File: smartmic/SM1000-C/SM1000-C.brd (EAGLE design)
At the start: 65 x 100 mm, 200 parts, among them CN1 HDR100-3, CN10 ST-3509, CN11 HDR100-3, CN12 DF11-16DS, CN2 MOLEX-MINI-B-SMT, CN3 RASM722PX, CN4 RJ-45, CN5 ST-3509, CN6 ST-3509, CN7 ST-3509, CN8 ST-3509, CN9 ST-3509, J1 JMP-2PIN, J3 JMP-2PIN, J4 JMP-2PIN, P1 TPAD50, P10 TPAD50, P11 TPAD50, P12 TPAD50, P13 TPAD50, P14 TPAD50, P15 TPAD50, P16 TPAD50, P17 TPAD50, P18 TPAD50, P19 TPAD50, P2 TPAD50, P20 TPAD50, P3 TPAD50, P4 TPAD50, P5 TPAD50, P6 TPAD50, P7 TPAD50, P8 TPAD50, P9 TPAD50, SW1 SW-BOURNS-7914S, SW2 SW-BOURNS-7914S, SW3 DPDT, SW4 SW-BOURNS-7914S, SW5 SW-BOURNS-7914J, T1 SM-LP-5001, T2 SM-LP-5001, U1 STM32F405, U2 LD3985M33R, U3 STMPS2141, U4 EMIF02-USB03F2, U5 TPS54329E, U6 LMV341, U7 LMV341, U8 LM386M-1, U9 LMV341

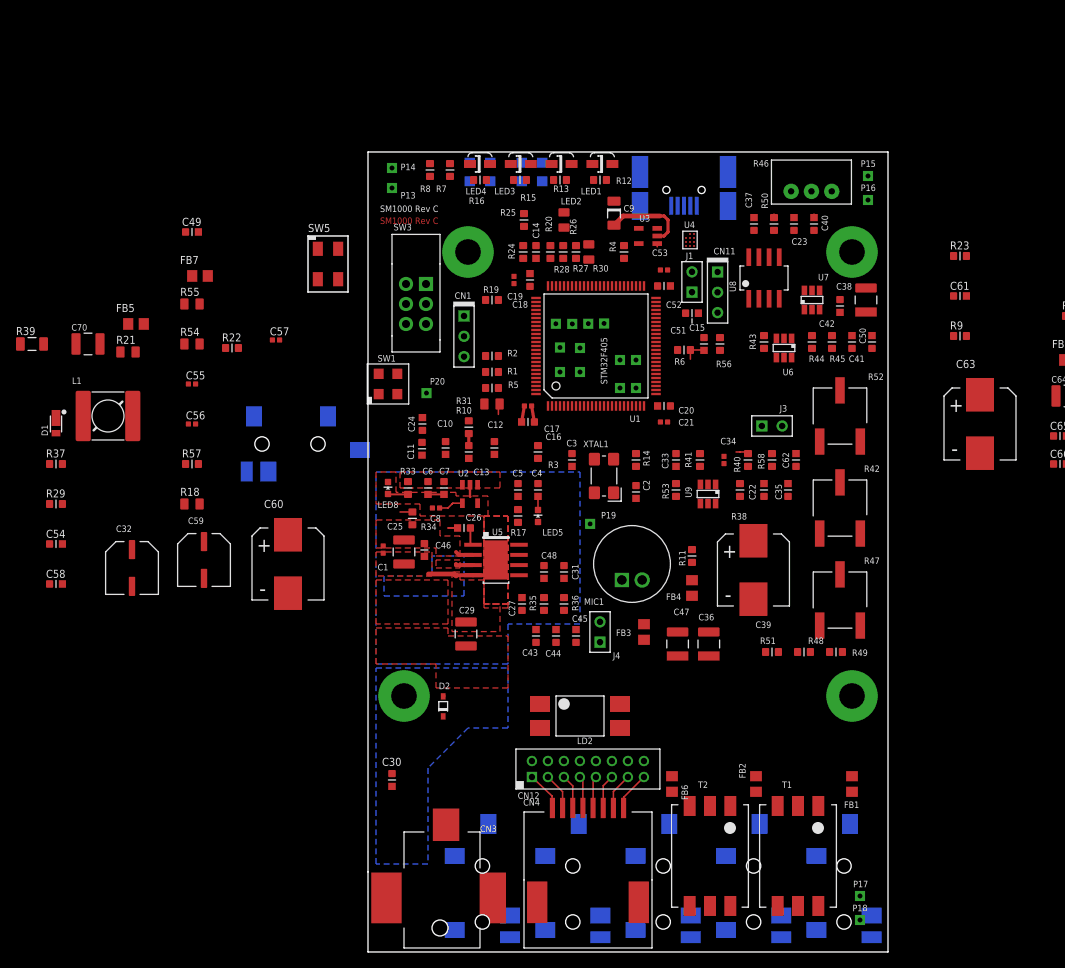
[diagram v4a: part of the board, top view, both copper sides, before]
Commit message: 10/24/2014 Update to Schematic, BOM & PCB - 10/24/2014  RGB Add Panasonic POTs Add Hirose A3C-16DA 2 x 8 female box header. Note: ST-3509 3.5mm connector cost unknown. Parts yet to be selected show $0.00 cost. Still need PTT switch selection.
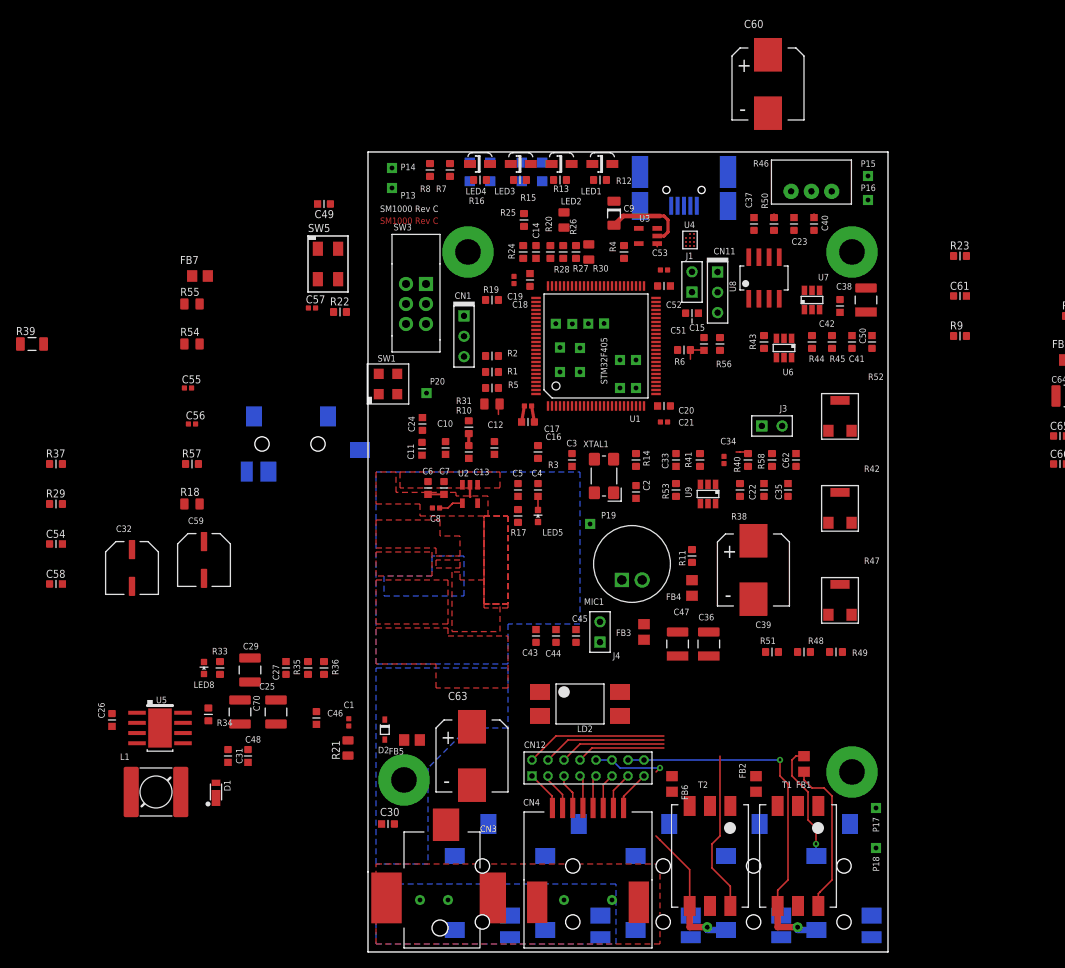
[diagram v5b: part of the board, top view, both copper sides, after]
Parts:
- removed DRILEGEND: (no value), drilegend:DRILEGEND
- CN12: value DF11-16DS -> HRS-A3C-16DA; device SM1000:HRS-DF11-16DS -> _RoweTel:HRS-A3C-16DA
- R42, R47, R52: device _RoweTel:POT3361 -> _RoweTel:PAN-EVM1D
- moved C60 84.9 mm to (50.0, 108.5)
- moved C63 75.9 mm to (13.0, 24.5)
- moved FB5 62.4 mm to (5.50, 26.5), turned to 180 degrees
- moved R21 56.6 mm to (-2.50, 25.5), turned to 90 degrees
- moved C26 50.1 mm to (-32.0, 29.0), turned to 270 degrees
- moved C70 49.8 mm to (-16.0, 30.0), turned to 270 degrees
- moved D1 49.2 mm to (-19.0, 20.5), turned to 180 degrees
- moved C31 47.9 mm to (-17.5, 24.5)
- moved L1 47.4 mm to (-26.5, 20.0)
- moved U5 47.0 mm to (-26.0, 28.0)
- moved C48 43.6 mm to (-15.0, 24.5)
- moved R34 35.4 mm to (-19.9, 29.7)
- moved R33 32.5 mm to (-18.5, 35.5)
- moved LED8 32.2 mm to (-20.5, 35.5)
- moved R36 31.0 mm to (-5.50, 35.5)
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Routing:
- net RF_SPKR: track 0.00 -> 46.0 mm, vias 0 -> 2
- net RF_MIC: track 0.00 -> 27.2 mm, vias 0 -> 2
- net GND: track 47.9 -> 22.2 mm, vias 0 -> 4
- net N$78: track 0.00 -> 20.1 mm
- net N$33: track 0.00 -> 19.8 mm
- net SPKR: track 0.00 -> 17.7 mm
- net MIC: track 0.00 -> 15.5 mm
- net N$64: track 0.00 -> 15.0 mm, vias 0 -> 1
- net APTT: track 0.00 -> 13.3 mm
- net N$81: track 69.2 -> 57.6 mm
- net RF_PTT: track 0.00 -> 11.1 mm
- net VDD: track 15.1 -> 4.10 mm
- net SW: track 3.46 -> 0.00 mm
- net N$47: track 2.52 -> 0.00 mm
- net N$21: track 2.42 -> 0.00 mm
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- removed copper zone on layer 2, net RF
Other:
- board text removed: "SM1000-REV-B- DRILL TABLE"

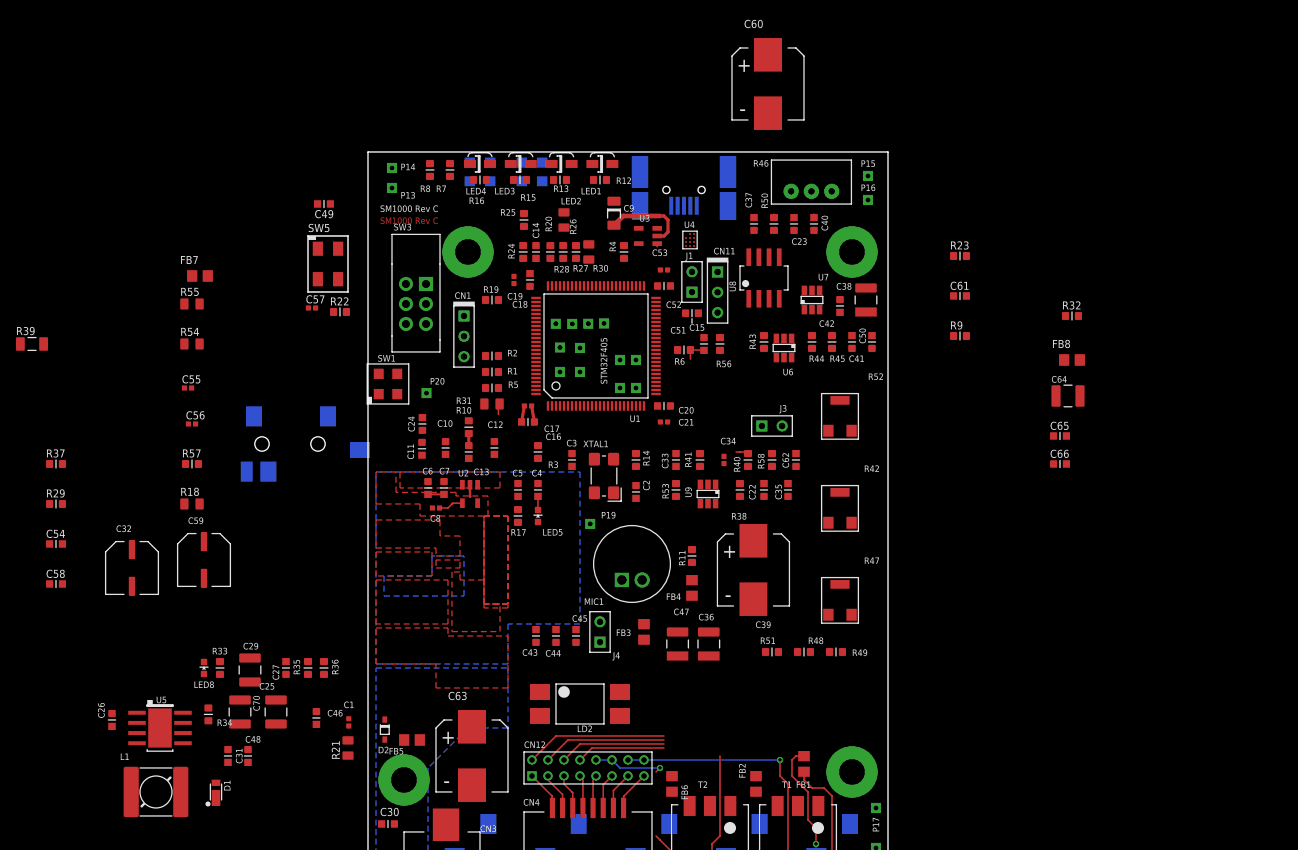
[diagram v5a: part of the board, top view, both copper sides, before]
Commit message: Update schematic & BOM to reflect latest part changes - rgb
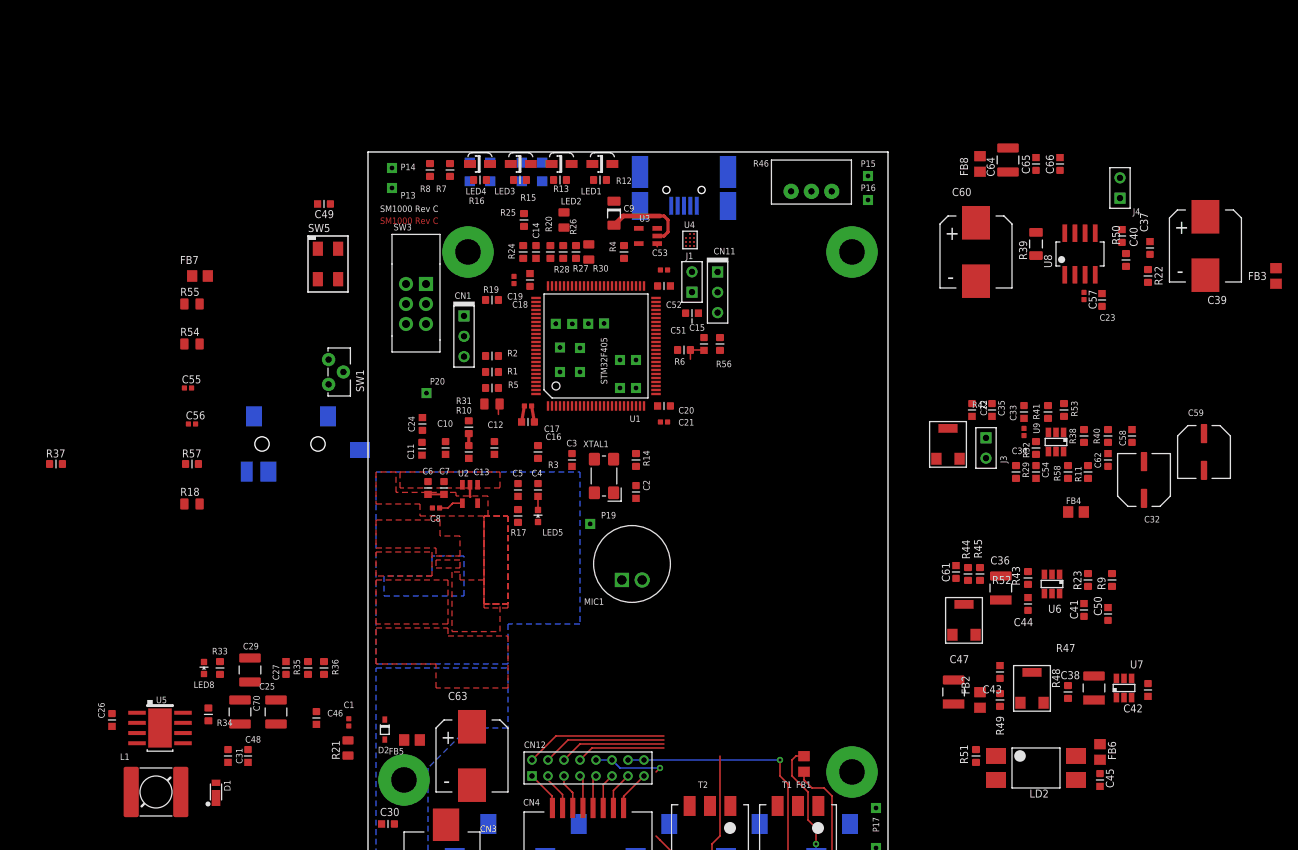
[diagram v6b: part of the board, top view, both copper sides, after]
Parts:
- SW1: value SW-BOURNS-7914S -> TS-026; device SM1000-2L-70x90:SW-BOURNS-7914S -> _RoweTel:TS-026
- moved C58 135.8 mm to (95.5, 64.5), turned to 90 degrees
- moved C32 127.0 mm to (97.0, 59.0), turned to 180 degrees
- moved R39 126.1 mm to (83.5, 88.5), turned to 90 degrees
- moved C59 125.7 mm to (104.5, 62.5)
- moved C54 122.8 mm to (83.5, 60.0), turned to 270 degrees
- moved R29 120.1 mm to (81.0, 60.0), turned to 270 degrees
- moved R22 101.1 mm to (97.5, 84.5), turned to 270 degrees
- moved C57 96.5 mm to (89.5, 82.0), turned to 270 degrees
- moved FB3 90.7 mm to (113.5, 84.5)
- moved J4 85.5 mm to (94.0, 95.5)
- moved C39 69.5 mm to (104.7, 88.2)
- moved C45 67.9 mm to (91.5, 21.5), turned to 270 degrees
- moved U7 62.2 mm to (94.5, 33.0)
- moved C42 61.5 mm to (97.5, 32.8)
- moved C44 59.1 mm to (82.5, 43.5)
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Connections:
- net GND: now also CN10.A
- net N$14: now also SW1.3; no longer SW1.1
- net N$75: now also CN8.B
- net VDD: now also SW1.1; no longer SW1.3, SW1.4
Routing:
- net N$46: track 1.58 -> 0.00 mm
- net N$43: track 0.90 -> 0.00 mm

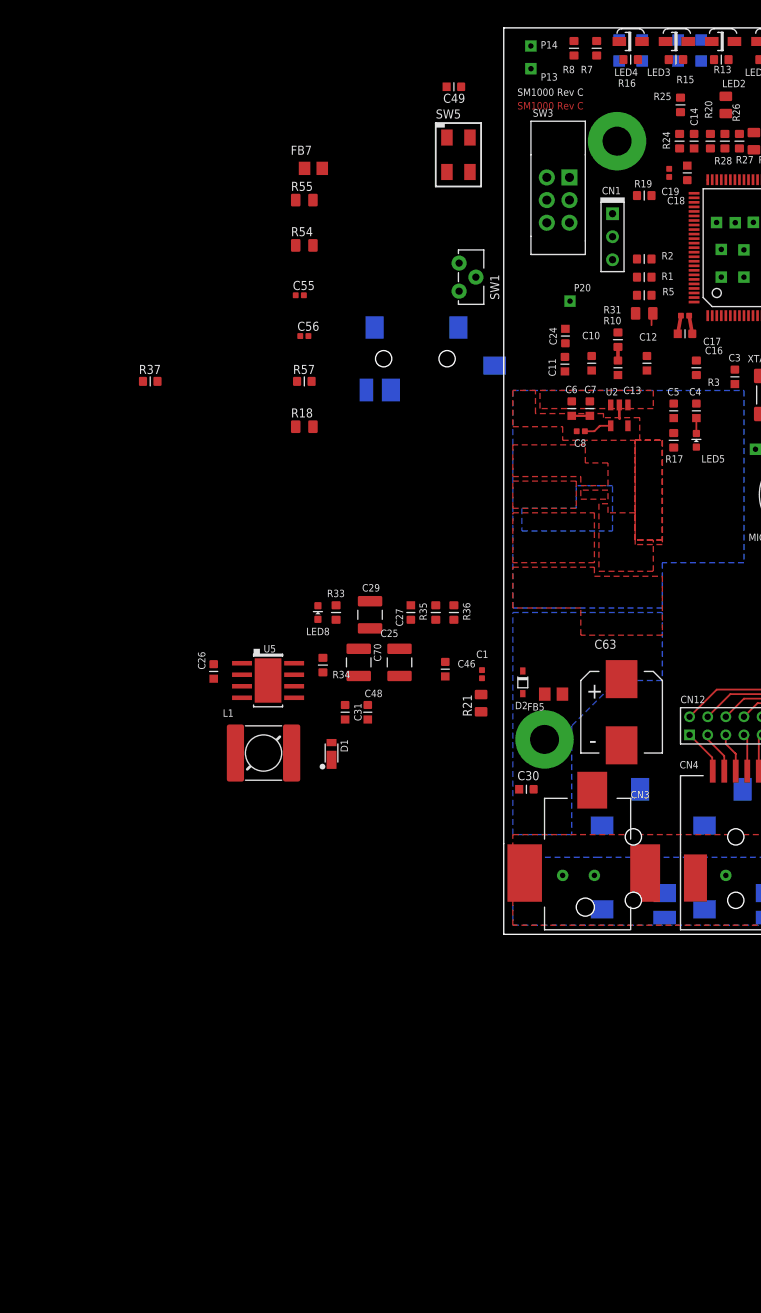
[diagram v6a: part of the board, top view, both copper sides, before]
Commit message: Correct errors in last upload - RGB
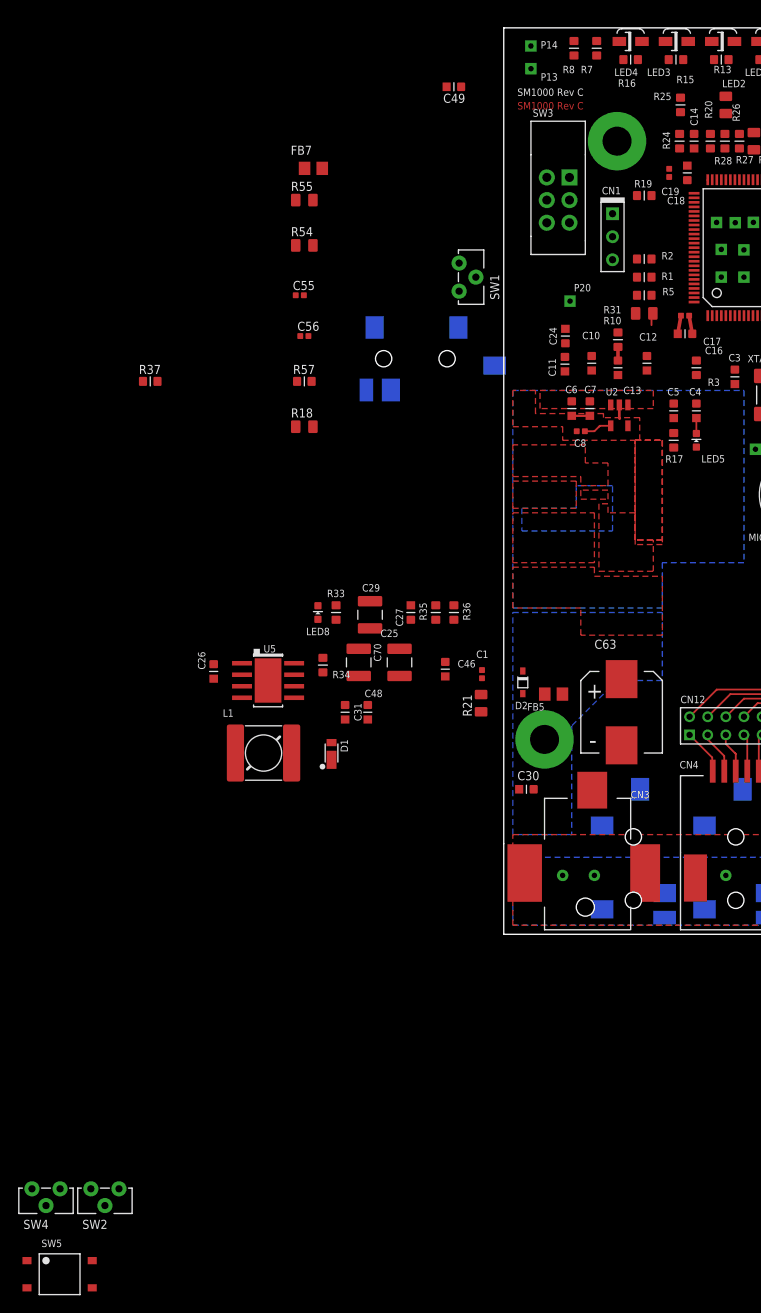
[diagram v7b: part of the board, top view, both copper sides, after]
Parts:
- SW2, SW4: value SW-BOURNS-7914S -> TS-026; device SM1000-2L-70x90:SW-BOURNS-7914S -> _RoweTel:TS-026
- SW5: value SW-BOURNS-7914J -> TS-02B; device SM1000:SW-BOURNS-7914J -> _RoweTel:TS-02B
- moved SW4 145.1 mm to (-50.5, -29.0), flipped to the top
- moved SW2 139.2 mm to (-44.0, -29.0), flipped to the top
- moved SW5 131.1 mm to (-49.0, -37.5)
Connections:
- net !BACK!: now also SW4.1; no longer SW4.3, SW4.4
- net !SELECT!: now also SW2.1; no longer SW2.3, SW2.4
- net GND: now also SW1.3, SW2.3, SW4.3; no longer SW2.1, SW4.1
- net N$14: no longer SW1.3

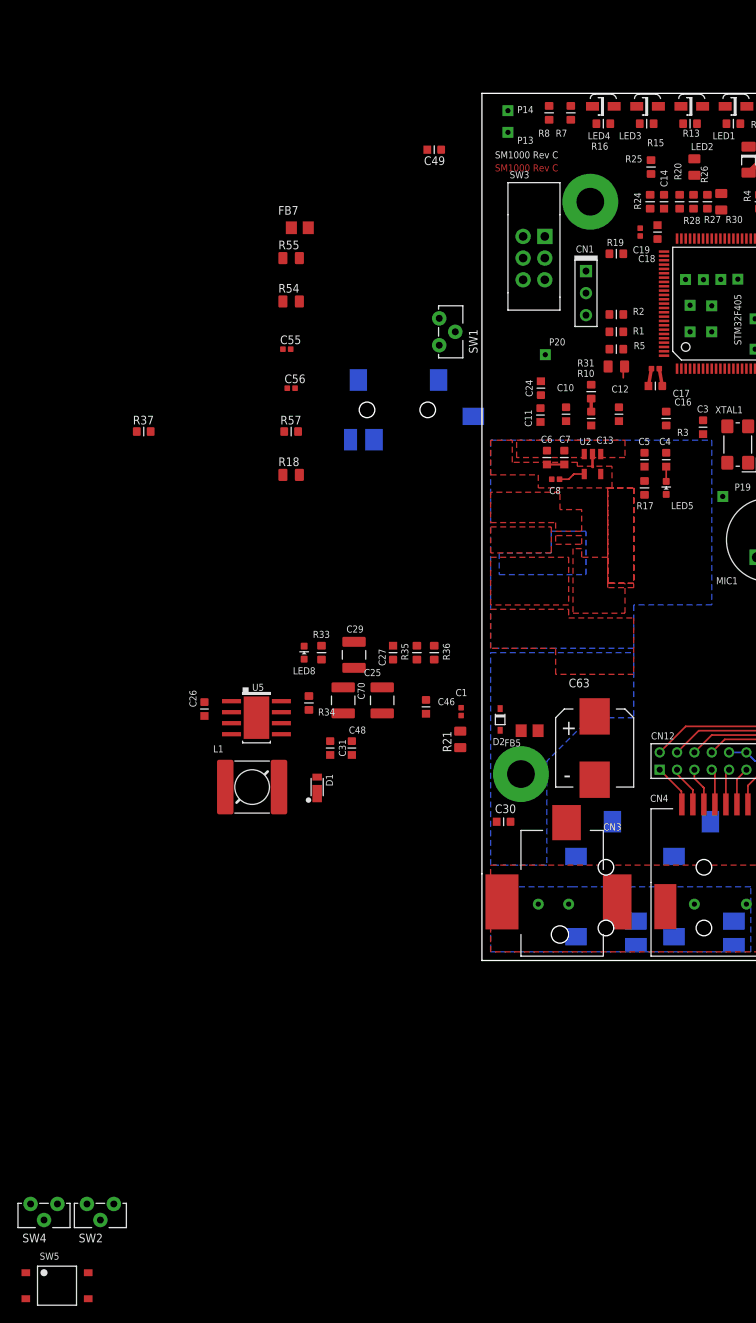
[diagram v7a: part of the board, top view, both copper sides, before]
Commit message: Update Schematic & BOM for new Power Connector and Speaker - RGB
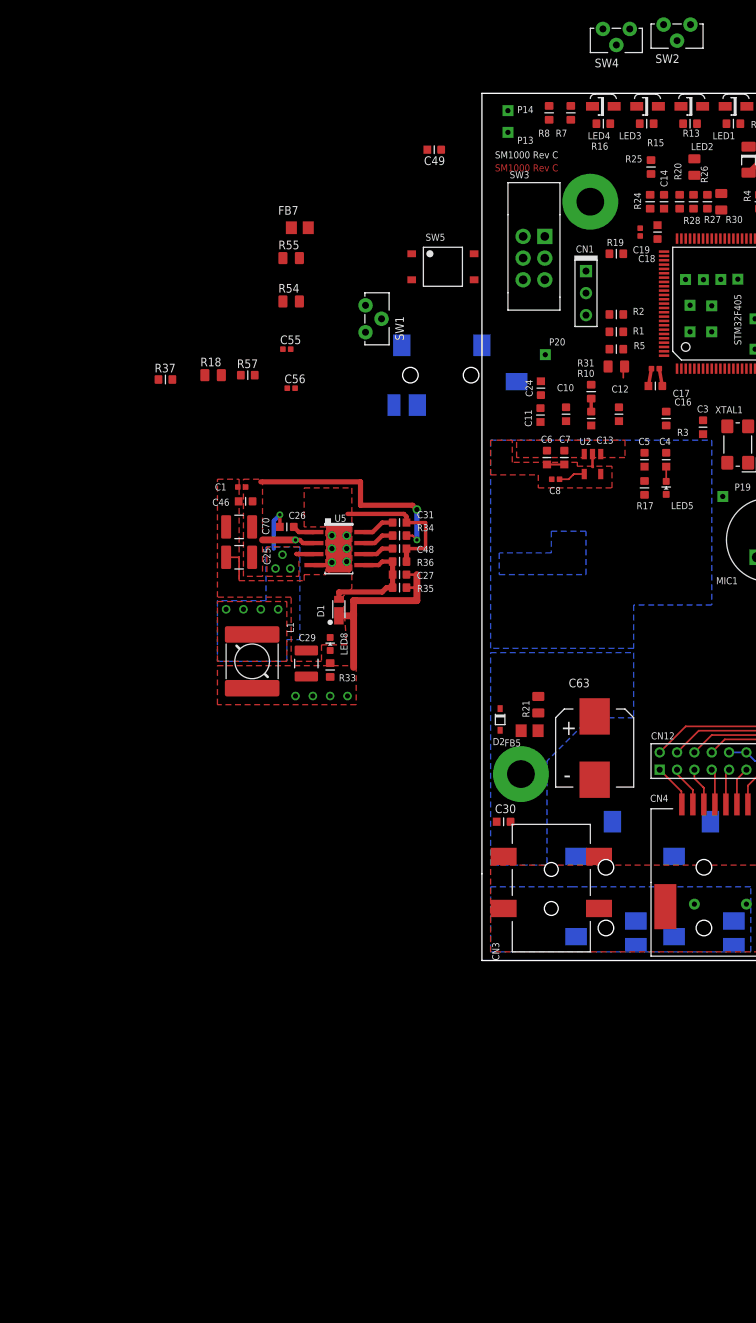
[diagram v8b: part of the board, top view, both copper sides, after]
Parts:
- added U$4: (no value), _RoweTel:SWPS-OTL
- CN3: value RASM722PX -> DS-0518; device _RoweTel:RASM722PX -> _RoweTel:DS-0518
- SPKR1: value SPKR -> SPKR-HY4004M-001
- moved SW2 151.4 mm to (22.5, 107.0)
- moved SW4 150.7 mm to (15.5, 106.5)
- moved SW5 125.6 mm to (-4.50, 80.0)
- moved C1 36.2 mm to (-27.7, 54.6), turned to 0 degrees
- moved C46 31.5 mm to (-27.2, 53.0), turned to 180 degrees
- moved C31 27.2 mm to (-9.50, 50.5), turned to 0 degrees
- moved C48 23.6 mm to (-9.50, 47.5), turned to 0 degrees
- moved C25 23.3 mm to (-28.0, 46.5), turned to 180 degrees
- moved C70 23.3 mm to (-28.0, 50.0), turned to 180 degrees
- moved C26 23.0 mm to (-22.5, 50.0), turned to 180 degrees
- moved R34 21.9 mm to (-9.50, 49.0), turned to 180 degrees
- moved U5 21.7 mm to (-16.5, 47.5)
- moved D1 20.7 mm to (-16.5, 41.0)
- moved R18 14.6 mm to (-31.0, 67.5)
- moved L1 14.5 mm to (-26.5, 34.5), turned to 270 degrees
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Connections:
- net GND: now also CN3.2; no longer CN3.1, CN3.3
- net N$77: now also CN3.1; no longer CN3.2
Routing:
- net GND: track 21.8 -> 56.6 mm, vias 4 -> 8
- net N$36: track 0.00 -> 31.9 mm, vias 0 -> 3
- net +5V: track 53.0 -> 75.3 mm, vias 0 -> 4
- net N$30: track 0.00 -> 13.7 mm
- net SW: track 0.00 -> 7.63 mm, vias 0 -> 8
- net N$38: track 0.00 -> 3.78 mm
- net N$42: track 0.00 -> 3.68 mm
- net N$40: track 0.00 -> 3.59 mm
- net N$21: track 0.00 -> 2.57 mm
- added copper zone on layer 1, net N$36
- removed copper zone on layer 1, net +VIN
